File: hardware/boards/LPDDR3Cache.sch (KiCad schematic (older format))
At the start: 2 parts

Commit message: Updated part mfr and added the proper part numbers
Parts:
- U? (x2): MFR (none) -> Lattice; MPN (none) -> LFE5UM5G-85F-8BG381I
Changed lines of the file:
@@
 F 2 "" H 4500 1950 50  0001 C CNN
 F 3 "" H 4500 1950 50  0001 C CNN
+F 4 "Lattice" H 5850 1800 50  0001 C CNN "MFR"
+F 5 "LFE5UM5G-85F-8BG381I" H 5850 1800 50  0001 C CNN "MPN"
 	6    5850 1800
 	1    0    0    -1
@@
 F 2 "" H 4550 4100 50  0001 C CNN
 F 3 "" H 4550 4100 50  0001 C CNN
+F 4 "Lattice" H 5900 3950 50  0001 C CNN "MFR"
+F 5 "LFE5UM5G-85F-8BG381I" H 5900 3950 50  0001 C CNN "MPN"
 	7    5900 3950
 	1    0    0    -1

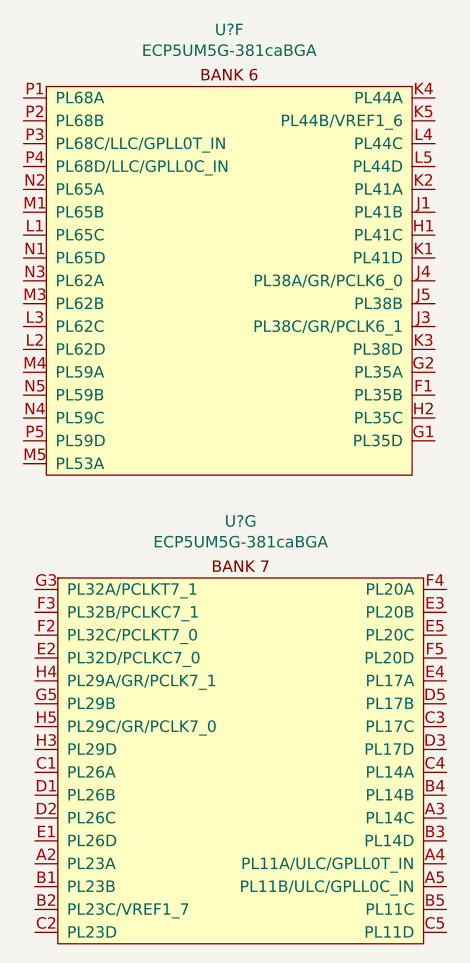
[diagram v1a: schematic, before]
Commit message: Did some annotation and fixed the FPGA bank that was accidentally labled as the cypress part
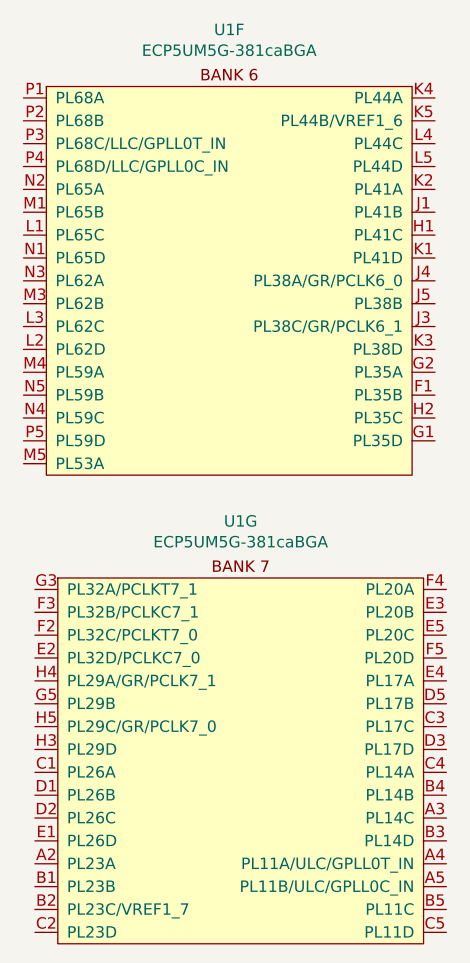
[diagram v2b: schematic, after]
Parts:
- U1: renamed from U?; footprint (none) -> lethalbit:318caBGA
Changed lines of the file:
@@
 $EndDescr
 $Comp
-L lethalbit:ECP5UM5G-381caBGA U?
+L lethalbit:ECP5UM5G-381caBGA U1
 U 6 1 5F1BFFB3
 P 5850 1800
-F 0 "U?" H 5850 2148 50  0000 C CNN
+F 0 "U1" H 5850 2148 50  0000 C CNN
 F 1 "ECP5UM5G-381caBGA" H 5850 2057 50  0000 C CNN
-F 2 "" H 4500 1950 50  0001 C CNN
+F 2 "lethalbit:318caBGA" H 4500 1950 50  0001 C CNN
 F 3 "" H 4500 1950 50  0001 C CNN
 F 4 "Lattice" H 5850 1800 50  0001 C CNN "MFR"
@@
 $EndComp
 $Comp
-L lethalbit:ECP5UM5G-381caBGA U?
+L lethalbit:ECP5UM5G-381caBGA U1
 U 7 1 5F1BFFB9
 P 5900 3950
-F 0 "U?" H 5900 4298 50  0000 C CNN
+F 0 "U1" H 5900 4298 50  0000 C CNN
 F 1 "ECP5UM5G-381caBGA" H 5900 4207 50  0000 C CNN
-F 2 "" H 4550 4100 50  0001 C CNN
+F 2 "lethalbit:318caBGA" H 4550 4100 50  0001 C CNN
 F 3 "" H 4550 4100 50  0001 C CNN
 F 4 "Lattice" H 5900 3950 50  0001 C CNN "MFR"

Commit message: Some more mist schematic edits
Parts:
- U1: DIGIKEY_PN (none) -> 220-2112-ND
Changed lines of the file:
@@
 F 4 "Lattice" H 5850 1800 50  0001 C CNN "MFR"
 F 5 "LFE5UM5G-85F-8BG381I" H 5850 1800 50  0001 C CNN "MPN"
+F 6 "220-2112-ND" H 5850 1800 50  0001 C CNN "DIGIKEY_PN"
 	6    5850 1800
 	1    0    0    -1
@@
 F 4 "Lattice" H 5900 3950 50  0001 C CNN "MFR"
 F 5 "LFE5UM5G-85F-8BG381I" H 5900 3950 50  0001 C CNN "MPN"
+F 6 "220-2112-ND" H 5900 3950 50  0001 C CNN "DIGIKEY_PN"
 	7    5900 3950
 	1    0    0    -1

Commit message: Some strugglebusting on getting the ERC errors cleaned up a bit
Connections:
- no-connect marks 0 -> 65
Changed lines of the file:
@@
 	1    0    0    -1
 $EndComp
+NoConn ~ 4950 1750
+NoConn ~ 4950 1850
+NoConn ~ 4950 1950
+NoConn ~ 4950 2050
+NoConn ~ 4950 2150
+NoConn ~ 4950 2250
+NoConn ~ 4950 2350
+NoConn ~ 4950 2450
+NoConn ~ 4950 2550
+NoConn ~ 4950 2650
+NoConn ~ 4950 2750
+NoConn ~ 4950 2850
+NoConn ~ 4950 2950
+NoConn ~ 4950 3050
+NoConn ~ 4950 3150
+NoConn ~ 4950 3250
+NoConn ~ 4950 3350
+NoConn ~ 6750 3250
+NoConn ~ 6750 3150
+NoConn ~ 6750 3050
+NoConn ~ 6750 2950
+NoConn ~ 6750 2850
+NoConn ~ 6750 2750
+NoConn ~ 6750 2650
+NoConn ~ 6750 2550
+NoConn ~ 6750 2450
+NoConn ~ 6750 2350
+NoConn ~ 6750 2250
+NoConn ~ 6750 2150
+NoConn ~ 6750 2050
+NoConn ~ 6750 1950
+NoConn ~ 6750 1850
+NoConn ~ 6750 1750
+NoConn ~ 5000 3900
+NoConn ~ 5000 4000
+NoConn ~ 5000 4100
+NoConn ~ 5000 4200
+NoConn ~ 5000 4300
+NoConn ~ 5000 4400
+NoConn ~ 5000 4500
+NoConn ~ 5000 4600
+NoConn ~ 5000 4700
+NoConn ~ 5000 4800
+NoConn ~ 5000 4900
+NoConn ~ 5000 5000
+NoConn ~ 5000 5100
+NoConn ~ 5000 5200
+NoConn ~ 5000 5300
+NoConn ~ 5000 5400
+NoConn ~ 6800 5400
+NoConn ~ 6800 5300
+NoConn ~ 6800 5200
+NoConn ~ 6800 5100
+NoConn ~ 6800 5000
+NoConn ~ 6800 4900
+NoConn ~ 6800 4800
+NoConn ~ 6800 4700
+NoConn ~ 6800 4600
+NoConn ~ 6800 4500
+NoConn ~ 6800 4400
+NoConn ~ 6800 4300
+NoConn ~ 6800 4200
+NoConn ~ 6800 4100
+NoConn ~ 6800 4000
+NoConn ~ 6800 3900
 $EndSCHEMATC
